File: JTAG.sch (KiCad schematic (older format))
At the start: 55 parts, among them CN5 CONN_RCPT_USB2.0_MINI_B_SMD_R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, CN6 2x5_Way_1.27mm_Pitch_Header, Q4 2N7002BK, Q5 2N7002BK, SW2 Switch_PB, U13 3_position_header, U15 FT2232HL-REEL, U16 74HC244, U18 3_position_header, U19 74HC244, U6 GW1N-9LQ100, U9 3_position_header, X2 ABM3B-12.000MHZ

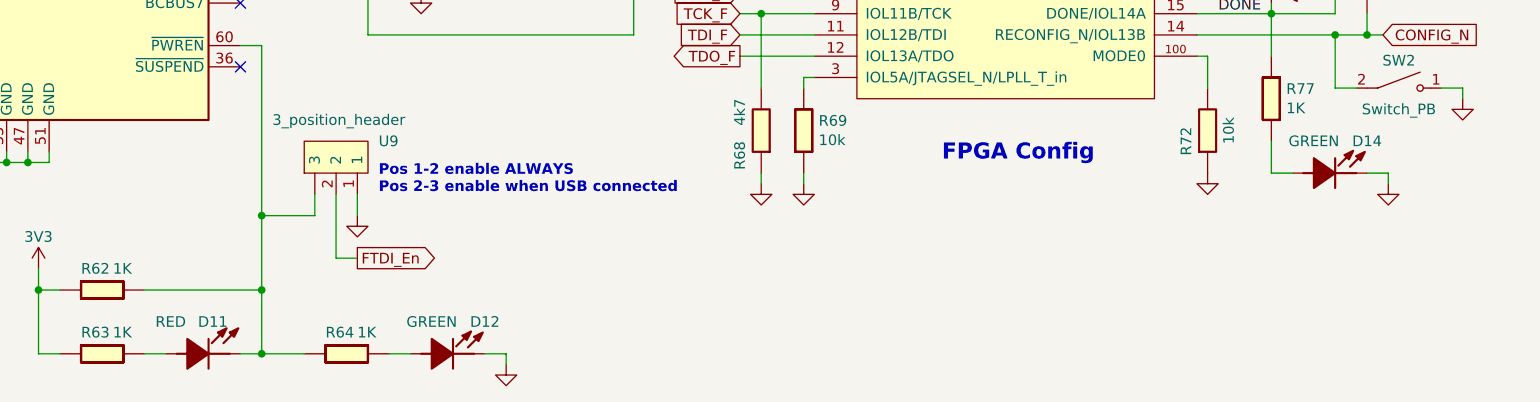
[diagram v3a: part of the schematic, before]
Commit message: add footprint
new footprint was added to parts without footprint
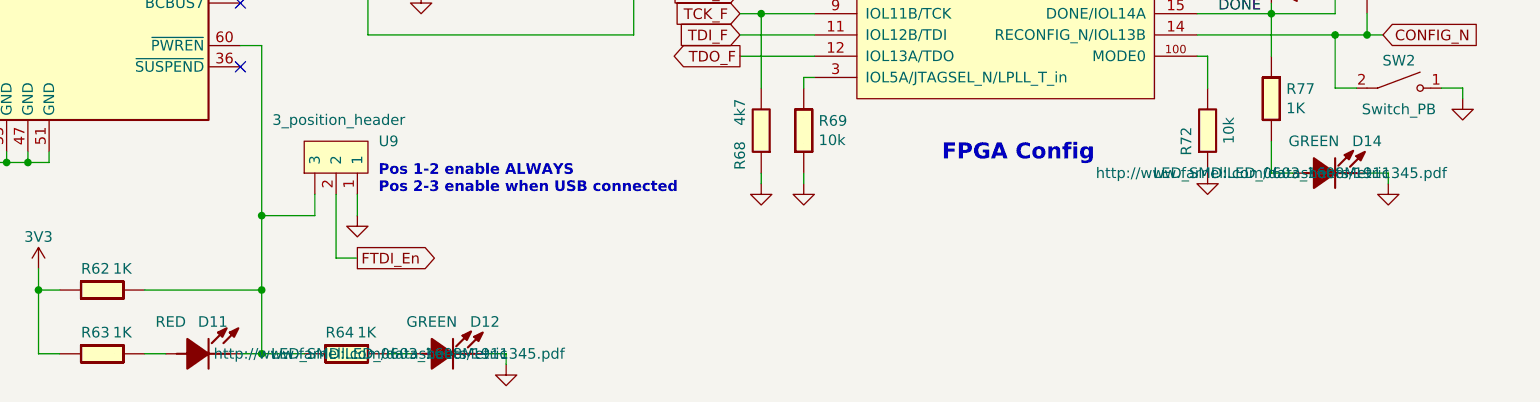
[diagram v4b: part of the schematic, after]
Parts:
- D12, D13, D14: footprint (none) -> LED_SMD:LED_0603_1608Metric
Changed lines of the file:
@@
 F 1 "Chip_Ferrite,_600R,_0603,_750mA" H 1800 1208 50  0001 C CNN
 F 2 "Inductor_SMD:L_0603_1608Metric" H 1500 900 50  0001 C CNN
-F 3 "" H 1500 900 50  0001 C CNN
+F 3 "http://www.farnell.com/datasheets/1756147.pdf" H 1500 900 50  0001 C CNN
 F 4 "600R" H 1700 1000 50  0000 C CNN "Val"
 F 5 "750mA" H 1950 1000 50  0000 C CNN "Current"
@@
 F 1 "Chip_Ferrite,_600R,_0603,_750mA" H 1800 1408 50  0001 C CNN
 F 2 "Inductor_SMD:L_0603_1608Metric" H 1500 1100 50  0001 C CNN
-F 3 "" H 1500 1100 50  0001 C CNN
+F 3 "http://www.farnell.com/datasheets/1756147.pdf" H 1500 1100 50  0001 C CNN
 F 4 "600R" H 1700 1050 50  0000 C CNN "Val"
 F 5 "750mA" H 1950 1050 50  0000 C CNN "Current"
@@
 F 0 "D13" V 10300 5150 50  0000 L CNN
 F 1 "LED_Red_0603_SMD" H 10100 5050 50  0001 C CNN
-F 2 "" H 10100 5050 50  0001 C CNN
-F 3 "" H 10100 5050 50  0001 C CNN
+F 2 "LED_SMD:LED_0603_1608Metric" H 10100 5050 50  0001 C CNN
+F 3 "http://www.farnell.com/datasheets/1911345.pdf" H 10100 5050 50  0001 C CNN
 F 4 "RED" V 10400 5150 50  0000 L CNN "Color"
 	1    10100 5050
@@
 F 0 "D14" H 10550 6450 50  0000 C CNN
 F 1 "LED_GREEN_0603_SMD" H 10100 6300 60  0001 C CNN
-F 2 "" H 10100 6300 50  0000 C CNN
-F 3 "" H 10100 6300 50  0000 C CNN
+F 2 "LED_SMD:LED_0603_1608Metric" H 10100 6300 50  0000 C CNN
+F 3 "http://www.farnell.com/datasheets/1911345.pdf" H 10100 6300 50  0000 C CNN
 F 4 "GREEN" H 10300 6450 50  0000 C CNN "Val"
 	1    10100 6300
@@
 F 0 "D12" H 6400 7300 50  0000 C CNN
 F 1 "LED_GREEN_0603_SMD" H 5950 7150 60  0001 C CNN
-F 2 "" H 5950 7150 50  0000 C CNN
-F 3 "" H 5950 7150 50  0000 C CNN
+F 2 "LED_SMD:LED_0603_1608Metric" H 5950 7150 50  0000 C CNN
+F 3 "http://www.farnell.com/datasheets/1911345.pdf" H 5950 7150 50  0000 C CNN
 F 4 "GREEN" H 6150 7300 50  0000 C CNN "Val"
 	1    5950 7150

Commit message: Update JTAG.sch
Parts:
- U6: symbol OpenVent-rescue:GW1N-9LQ100-OpenVent -> OpenVent-rescue:GW1N-9LQ100-OpenVent-OpenVent-rescue
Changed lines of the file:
@@
 	9800 5100 9800 5450
 $Comp
-L OpenVent-rescue:GW1N-9LQ100-OpenVent U?
+L OpenVent-rescue:GW1N-9LQ100-OpenVent-OpenVent-rescue U?
 U 2 1 6073BAD7
 P 8950 5350

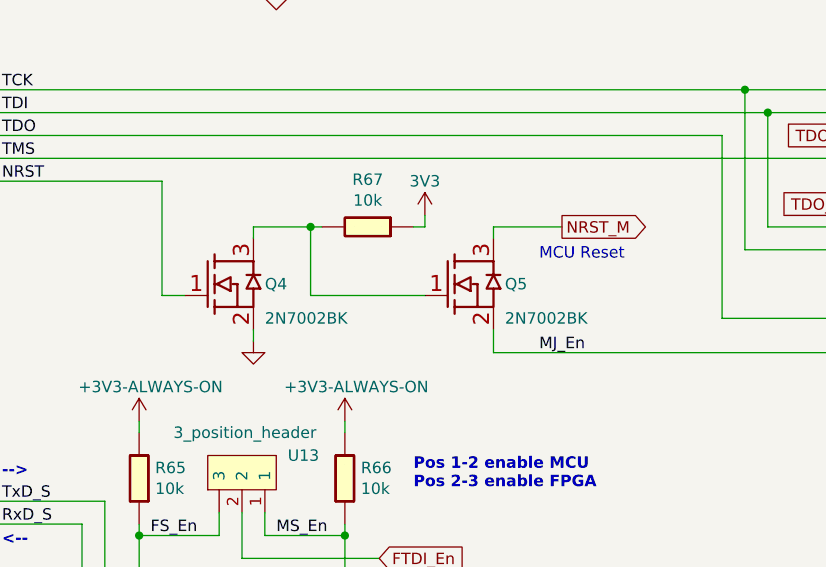
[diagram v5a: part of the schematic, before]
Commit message: Update JTAG.sch
Q4, Q5 replaced
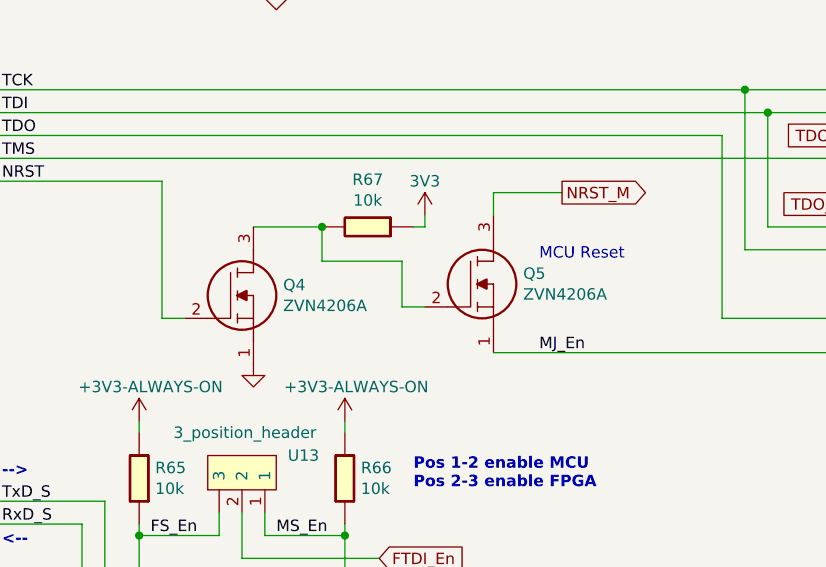
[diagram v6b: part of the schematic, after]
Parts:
- removed Q4, Q5: 2N7002BK, symbol OpenVent:2N7002BK
- added Q4, Q5: ZVN4206A, symbol OpenVent:ZVN4206A
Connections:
- wire segments 292 -> 290
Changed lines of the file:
@@
 MCU Reset
-Wire Wire Line
-	7650 3150 7650 3250
-Wire Wire Line
-	7650 2700 7950 2700
-$Comp
-L OpenVent:2N7002BK Q?
-U 1 1 60A00DDC
-P 7650 2750
-AR Path="/5F99D63D/60A00DDC" Ref="Q?"  Part="1"
-AR Path="/5F8F8987/60A00DDC" Ref="Q5"  Part="1"
-F 0 "Q5" H 7600 2550 50  0000 R CNN
-F 1 "2N7002BK" H 7600 2400 50  0000 R CNN
-F 2 "" H 7650 2750 50  0000 C CNN
-F 3 "" H 7650 2750 50  0000 C CNN
-	1    7650 2750
-	-1   0    0    -1
-$EndComp
-Wire Wire Line
-	7650 2750 7650 2700
-Wire Wire Line
-	6850 2700 6850 3000
 Wire Wire Line
 	3650 900  3650 1800
@@
 Wire Wire Line
 	5250 2400 9325 2400
-Wire Wire Line
-	6600 2700 6850 2700
-Wire Wire Line
-	6600 3150 6600 3200
-Wire Wire Line
-	6600 2750 6600 2700
-$Comp
-L OpenVent:2N7002BK Q?
-U 1 1 609635D6
-P 6600 2750
-AR Path="/5F99D63D/609635D6" Ref="Q?"  Part="1"
-AR Path="/5F8F8987/609635D6" Ref="Q4"  Part="1"
-F 0 "Q4" H 6550 2550 50  0000 R CNN
-F 1 "2N7002BK" H 6550 2400 50  0000 R CNN
-F 2 "" H 6600 2750 50  0000 C CNN
-F 3 "" H 6600 2750 50  0000 C CNN
-	1    6600 2750
-	-1   0    0    -1
-$EndComp
 $Comp
 L OpenVent:GND #PWR0107
 U 1 1 608A6626
-P 6600 3200
-F 0 "#PWR0107" H 6600 2950 50  0001 C CNN
-F 1 "GND" H 6600 3050 50  0001 C CNN
-F 2 "" H 6600 3200 50  0001 C CNN
-F 3 "" H 6600 3200 50  0001 C CNN
-	1    6600 3200
-	1    0    0    -1
-$EndComp
-Wire Wire Line
-	6200 3000 6300 3000
-Wire Wire Line
-	6200 2500 6200 3000
+P 6600 3300
+F 0 "#PWR0107" H 6600 3050 50  0001 C CNN
+F 1 "GND" H 6600 3150 50  0001 C CNN
+F 2 "" H 6600 3300 50  0001 C CNN
+F 3 "" H 6600 3300 50  0001 C CNN
+	1    6600 3300
+	1    0    0    -1
+$EndComp
 Wire Wire Line
 	1400 2100 2850 2100
@@
 Wire Wire Line
 	7350 2650 7350 2700
-Wire Wire Line
-	6850 3000 7350 3000
-Wire Wire Line
-	6850 2700 6900 2700
-Connection ~ 6850 2700
 Wire Wire Line
 	5250 2500 6200 2500
@@
 Connection ~ 5350 6500
 Connection ~ 5350 6850
-Text GLabel 7950 2700 2    50   Output ~ 0
+Text GLabel 7950 2550 2    50   Output ~ 0
 NRST_M
 $Comp
@@
 	800  3650 800  3750
 NoConn ~ 5250 5800
+$Comp
+L OpenVent:ZVN4206A Q4
+U 1 1 613C54CA
+P 6600 3100
+F 0 "Q4" H 6730 3246 50  0000 L CNN
+F 1 "ZVN4206A" H 6730 3155 50  0000 L CNN
+F 2 "" H 7150 2800 50  0001 C CNN
+F 3 "" H 7150 2800 50  0001 C CNN
+	1    6600 3100
+	1    0    0    -1
+$EndComp
+Wire Wire Line
+	6300 3100 6200 3100
+Wire Wire Line
+	6200 2500 6200 3100
+$Comp
+L OpenVent:ZVN4206A Q5
+U 1 1 6140EDDE
+P 7650 3050
+F 0 "Q5" H 7780 3196 50  0000 L CNN
+F 1 "ZVN4206A" H 7780 3105 50  0000 L CNN
+F 2 "" H 8200 2750 50  0001 C CNN
+F 3 "" H 8200 2750 50  0001 C CNN
+	1    7650 3050
+	1    0    0    -1
+$EndComp
+Wire Wire Line
+	7950 2550 7650 2550
+Wire Wire Line
+	7650 2550 7650 2650
+Wire Wire Line
+	7350 3050 7250 3050
+Wire Wire Line
+	7250 3050 7250 2850
+Wire Wire Line
+	7250 2850 6900 2850
+Wire Wire Line
+	6900 2850 6900 2700
+Wire Wire Line
+	6600 2700 6900 2700
+Connection ~ 6900 2700
 $EndSCHEMATC

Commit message: footprint added to 99%
99% of parts have footprint now.
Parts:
- CN5: footprint (none) -> OpenVent_Footprint_Test:CONN_RCPT_USB2.0_MICRO_B_SMD_R_A
- CN6: footprint (none) -> Connector_PinHeader_1.27mm:PinHeader_2x05_P1.27mm_Vertical
- U13, U18, U9: footprint (none) -> Connector_PinHeader_2.54mm:PinHeader_1x03_P2.54mm_Vertical
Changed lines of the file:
@@
 F 0 "CN5" H 1800 3900 60  0000 L BNN
 F 1 "CONN_RCPT_USB2.0_MINI_B_SMD_R_A" H 1400 3350 60  0001 C CNN
-F 2 "" H 1400 3350 60  0001 C CNN
+F 2 "OpenVent_Footprint_Test:CONN_RCPT_USB2.0_MICRO_B_SMD_R_A" H 1400 3350 60  0001 C CNN
 F 3 "" H 1400 3350 60  0001 C CNN
 	1    1400 3350
@@
 F 0 "U18" V 9650 700 50  0000 R CNN
 F 1 "3_position_header" V 9750 1200 50  0000 R CNN
-F 2 "" H 9550 1150 50  0001 C CNN
+F 2 "Connector_PinHeader_2.54mm:PinHeader_1x03_P2.54mm_Vertical" H 9550 1150 50  0001 C CNN
 F 3 "" H 9550 1150 50  0001 C CNN
 	1    9550 1150
@@
 F 0 "CN6" H 10000 3500 50  0000 C CNN
 F 1 "2x5_Way_1.27mm_Pitch_Header" H 9750 2800 50  0000 C CNN
-F 2 "" H 10000 3500 50  0001 C CNN
+F 2 "Connector_PinHeader_1.27mm:PinHeader_2x05_P1.27mm_Vertical" H 10000 3500 50  0001 C CNN
 F 3 "http://www.cnctech.us/idcmatching2.pdf" H 10000 3500 50  0001 C CNN
 	1    10000 3500
@@
 F 0 "U13" V 6400 3350 50  0000 R CNN
 F 1 "3_position_header" V 6500 3850 50  0000 R CNN
-F 2 "" H 6300 3800 50  0001 C CNN
+F 2 "Connector_PinHeader_2.54mm:PinHeader_1x03_P2.54mm_Vertical" H 6300 3800 50  0001 C CNN
 F 3 "" H 6300 3800 50  0001 C CNN
 	1    6300 3800
@@
 F 0 "U9" V 5550 5800 50  0000 R CNN
 F 1 "3_position_header" V 5650 6300 50  0000 R CNN
-F 2 "" H 5450 6250 50  0001 C CNN
+F 2 "Connector_PinHeader_2.54mm:PinHeader_1x03_P2.54mm_Vertical" H 5450 6250 50  0001 C CNN
 F 3 "" H 5450 6250 50  0001 C CNN
 	1    5450 6250

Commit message: Updated the project to include a M2GL010-1TQG144 IGLOO2 FPGA instead of the GOWIN. Since the IGLOO has some 2.5V BANKs as well as 3.3V Banks, some circuitry will need to be modified elsewhere in the circuit, but most of the interfaces are easily changeable, be it different power supplies or the additions of transistors or potential dividers. I will edit the rest of the design later, and write up a list of things I changed for the other peeps in the design team to review
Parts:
- added U?: M2GL010-TQ144, symbol OVB_Microsemi:M2GL010-TQ144
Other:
- note added: "Use this when the time comes"
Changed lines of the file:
@@
 EESchema Schematic File Version 4
-EELAYER 30 0
+LIBS:OpenVent-cache
+EELAYER 26 0
 EELAYER END
 $Descr A4 11693 8268
 encoding utf-8
-Sheet 6 8
+Sheet 5 9
 Title "OpenVent Control Board"
 Date "2020-10-20"
@@
 F 1 "LED_GREEN_0603_SMD" H 10100 6300 60  0001 C CNN
 F 2 "LED_SMD:LED_0603_1608Metric" H 10100 6300 50  0000 C CNN
-F 3 "http://www.farnell.com/datasheets/1911345.pdf" H 10100 6300 50  0000 C CNN
+F 3 "http://www.farnell.com/datasheets/1911345.pdf" H 9650 6150 50  0000 C CNN
 F 4 "GREEN" H 10300 6450 50  0000 C CNN "Val"
 	1    10100 6300
@@
 	6600 2700 6900 2700
 Connection ~ 6900 2700
+$Comp
+L OVB_Microsemi:M2GL010-TQ144 U?
+U 7 1 62025844
+P 8450 4150
+AR Path="/5F8F894A/62025844" Ref="U?"  Part="7"
+AR Path="/5F8F8987/62025844" Ref="U?"  Part="7"
+F 0 "U?" H 8531 4215 50  0000 C CNN
+F 1 "M2GL010-TQ144" H 8531 4124 50  0000 C CNN
+F 2 "" H 8450 4150 50  0001 C CNN
+F 3 "" H 8450 4150 50  0001 C CNN
+	7    8450 4150
+	1    0    0    -1
+$EndComp
+Wire Notes Line
+	8050 4000 8050 5050
+Wire Notes Line
+	9000 5050 9000 4000
+Wire Notes Line
+	9000 4000 8050 4000
+Wire Notes Line
+	8050 5050 9000 5050
+Text Notes 7950 4000 0    50   ~ 0
+Use this when the time comes
 $EndSCHEMATC
